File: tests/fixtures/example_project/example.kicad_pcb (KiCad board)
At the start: 2 copper layers, 40 x 30 mm, 5 parts, among them J1 Conn_01x03_Pin, U1 LM321

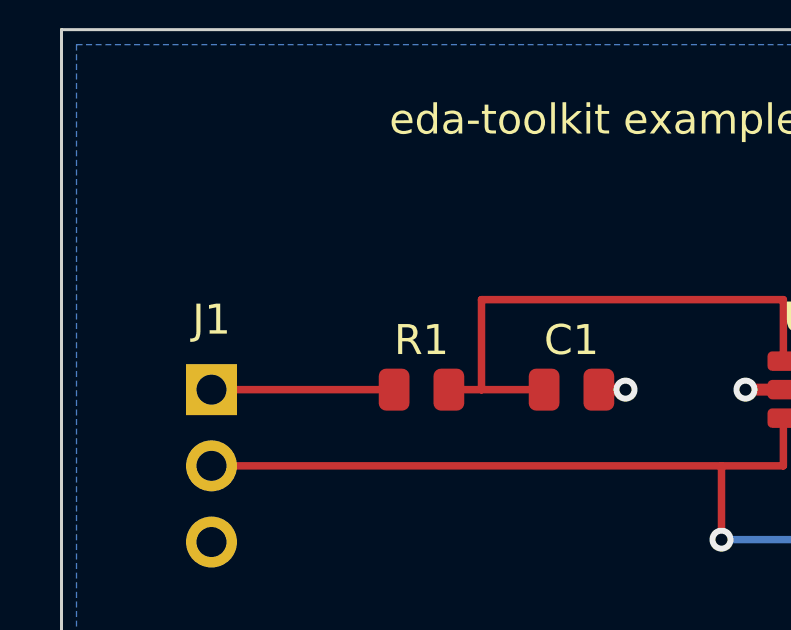
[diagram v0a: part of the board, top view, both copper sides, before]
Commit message: Make the generator draw power the way a reader expects, and the board say what it is
The reviewer's second pass, generalised into the toolkit. On the sheet:
power symbols stand upright (rails up, grounds down) on jogs, sidesteps
or per-side bus columns; PWR_FLAG sits beside the net's source instead
of on a label row; passives show their voltage/tolerance/power ratings
beside the symbol. On the board: ground pours on both faces with a
stitching ring around the rim so no edge copper floats, silkscreen
carries the board name and revision, connector pins are labelled in
silk, indicator LEDs say what they indicate, and the buck gets an
explicit high-current ground return sized like its outbound path.

Rules to check what checks: readability.power_symbol_orientation,
route.right_angle, silk.missing_board_id, silk.unlabeled_connector,
layout.pour_single_sided - each calibrated over the 18 demo projects
and graded info where half of human-drawn boards fire it. The pour rule
is context, not blocking: the test fixture itself is single-sided.

The stitching ring existed but never reached a board: resolve_routes
returned early for designs with no auto tracks - which is all of them -
before the line that appends it. Both paths stitch now.

Co-Authored-By: Claude Fable 5 <noreply@anthropic.com>
Claude-Session: https://claude.ai/code/session_01DUj7Ltu92tWg159mCSacwY
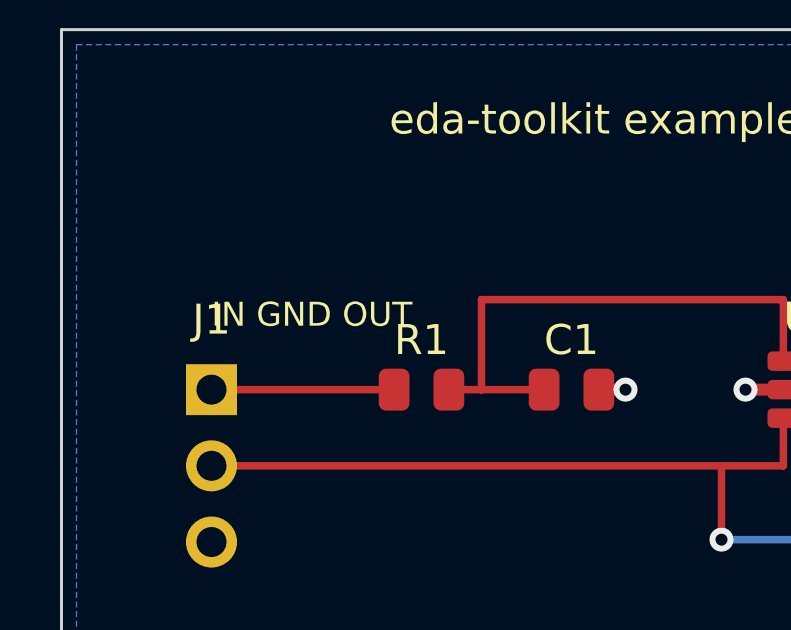
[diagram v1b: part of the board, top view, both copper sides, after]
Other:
- board text added: "IN GND OUT"
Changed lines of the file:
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@@
 		(layer "Edge.Cuts")
+	)
+	(gr_text "IN GND OUT"
+		(at 105 89.5 0)
+		(layer "F.SilkS")
+		(effects
+			(font
+				(size 0.8 0.8)
+				(thickness 0.12)
+			)
+			(justify left)
+		)
 	)
 	(gr_text "eda-toolkit example board"

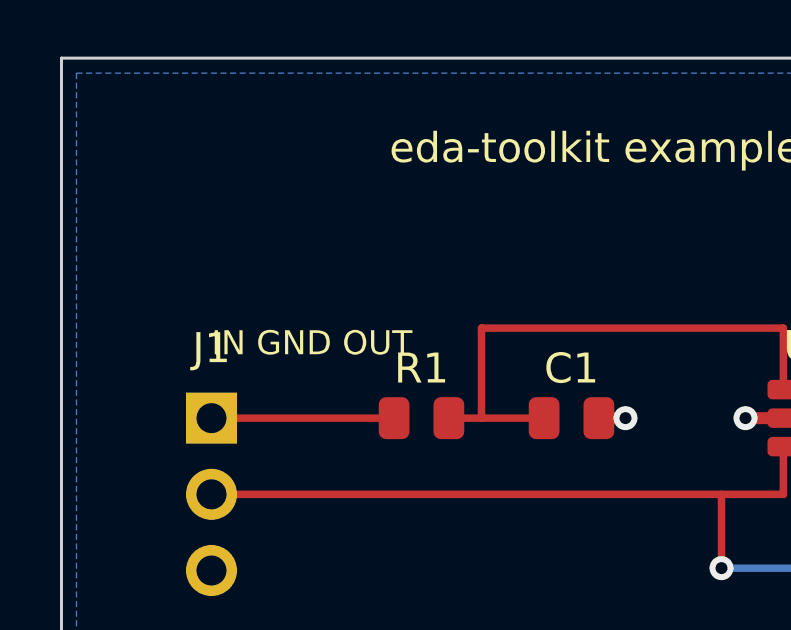
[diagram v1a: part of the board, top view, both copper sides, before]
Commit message: Rip up copper that tours, and put a footprint's zones where the footprint is
The plots showed three things on the artwork side that no rule reported.

**A track that goes round the board to cover thirteen millimetres.** The
op-amp's feedback wrap had to get from one side of a SOT-23-5 to the other
and, routed last, took fifty-six millimetres of tour because everything
nearer was already spoken for. That is an ordering problem, so the loop that
fixes ordering fixes it: `_route_all` now reports what each track cost
against `route.wander`'s own baseline - imported, not copied, so the two
cannot drift - and the worst tour goes to the front and the set is routed
again. A track that still tours from first pick has nowhere better to be and
is left alone. The default order is shortest-first for the same reason: a
thirteen millimetre connection has few ways to be made and a forty
millimetre one has many. The learned order is now written on every change,
not only on success, because an afternoon of rip-ups is worth keeping when
the machine goes away in the middle.

**A keep-out sitting at the origin.** A footprint may carry zones of its own
and KiCad stores *those* in board coordinates while everything else in a
footprint is stored relative to it. The Pico module's two pad keep-outs had
been at (0, -6) for four rounds - off the board, keeping nothing out. DRC is
silent because an empty region violates no rule, and the only visible sign
was the plot: "fit to page" fits the bounding box, so every view of that
board came out at half scale in one corner with the rest blank.
`layout.zone_outside_outline` reports it; the placer moves it.

**Silkscreen printed through silkscreen.** The schematic has
`readability.text_over_text` and the board had nothing, though the board is
the harder case - a sheet can be zoomed and a bare board cannot.
`silk.text_over_text` measures it from the font size the file states; on
KiCad's demo boards it fires on 6 of 16, 173 times. The generator places t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
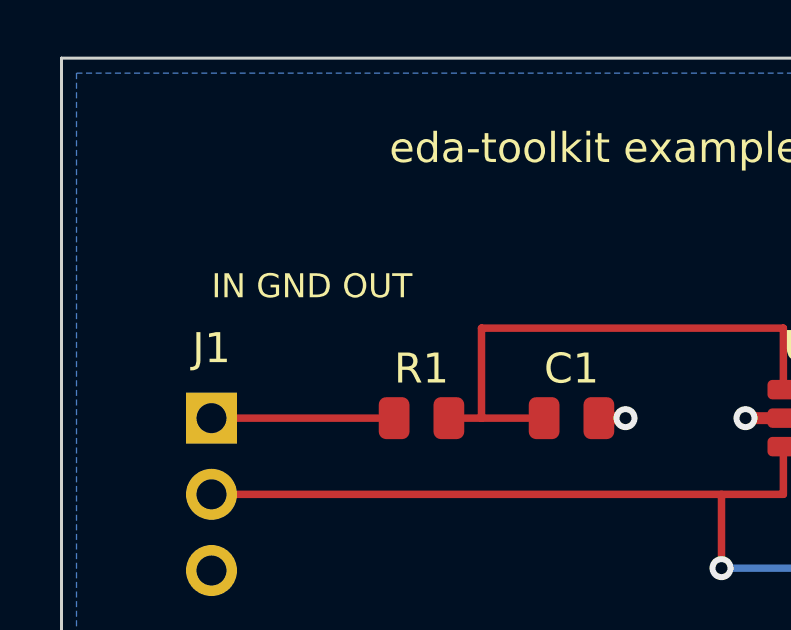
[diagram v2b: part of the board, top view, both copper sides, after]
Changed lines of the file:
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@@
 	)
 	(gr_text "IN GND OUT"
-		(at 105 89.5 0)
+		(at 105 87.6 0)
 		(layer "F.SilkS")
 		(effects

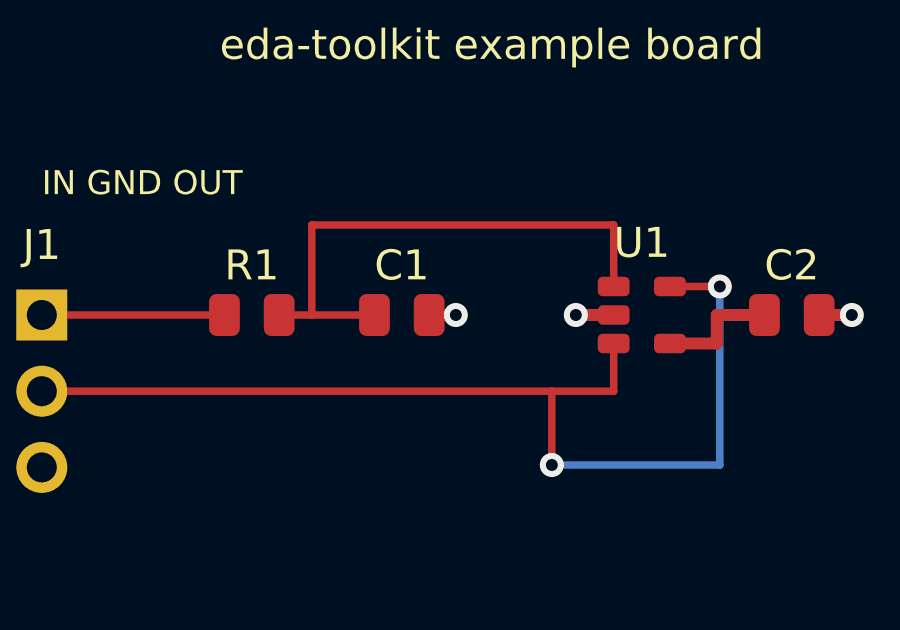
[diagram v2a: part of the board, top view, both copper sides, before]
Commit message: Keep vias out of the lands they would drain
The reviewer's next one, and it is not one board's problem: vias were
landing inside surface-mount lands across the set. A hole in a land is a
hole solder wicks down during reflow - the joint above it starves, and
nothing on the assembled board tells that apart from a cold one.
Via-in-pad is a real technique and a filled-and-capped process, not a
drawing; a layout that has not specified the process may not draw it.

The router was the source. `_blocked` skips a route's own net, so
nothing stopped a layer change from happening on the very land the route
started at, and eighteen vias across three boards sat in one. Pads are
now marked as pads in the obstacle list and every one of them, whoever
owns it, is a cell where a via may not go - so an escape that has to
reach the plane leaves the land first and turns its via beside it. The
stitching pass kept ground vias a via-radius from ground lands where it
kept signal ones a radius plus clearance; both are the same distance
now, because the plane gains nothing from touching a land it can reach a
stub away.

`via.in_pad` measures the copper gap from every via to every land and
reports what is left. The exposed thermal pad under a package is exempt
- the via array in one is the datasheet's own answer, and nothing a
signal reaches is four square millimetres. It blocks under the
ai-generated policy: a generated board has no reason to draw this.

The test fixture had one too, a via twenty-five microns into C1's ground
land; it moves three tenths of a millimetre and the board is DRC clean
on both matrix versions as before.

Co-Authored-By: Claude Fable 5 <noreply@anthropic.com>
Claude-Session: https://claude.ai/code/session_01DUj7Ltu92tWg159mCSacwY
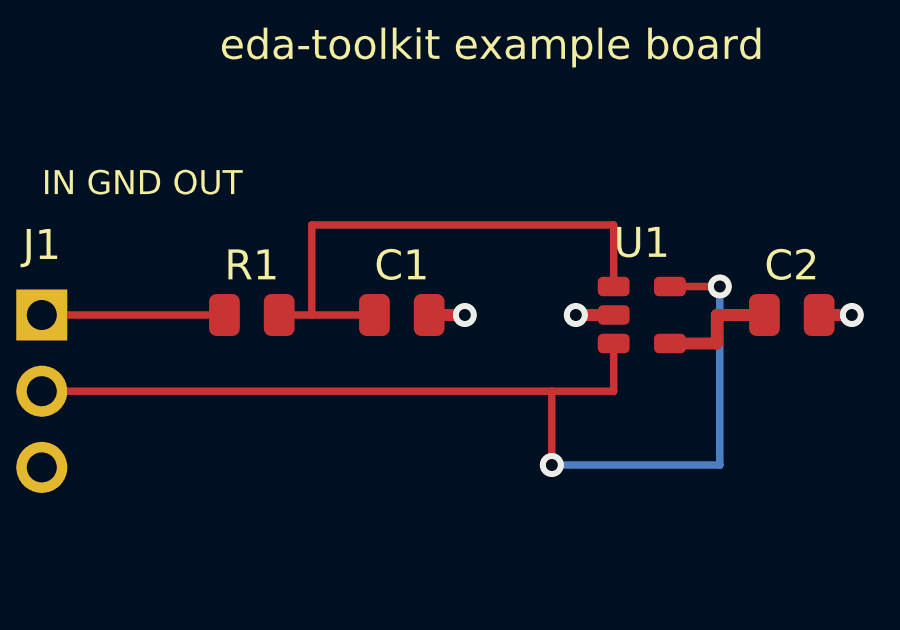
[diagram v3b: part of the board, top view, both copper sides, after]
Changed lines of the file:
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@@
 	(segment
 		(start 117.9125 92)
-		(end 118.8 92)
+		(end 119.1 92)
 		(width 0.4)
 		(layer "F.Cu")
@@
 	)
 	(via
-		(at 118.8 92)
+		(at 119.1 92)
 		(size 0.8)
 		(drill 0.4)
